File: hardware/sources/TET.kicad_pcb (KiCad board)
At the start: 4 copper layers, 90.2 x 95.9 mm, 80 parts, among them J1 SWT, M1 MountingHole, M2 MountingHole, M3 MountingHole, M4 MountingHole, U1 E80-900M2213S_C42464134, U10 STM32L431RBT6TR, U12 TCAN330GDCNR, U13 SMA_1, U14 SMA_2, U15 8 MHz, U16 5015, U17 5015, U18 5015, U19 INA226AIDGSR, U2 STM32L431CBT6, U20 TLV75533PDBVR, U3 W25Q128JVSIQTR, U4 W25Q128JVSIQTR, U5 W25Q128JVSIQTR, U6 TMP112AIDRLR, U7 TMP112AIDRLR, U8 TMP112AIDRLR, U9 TMP112AIDRLR

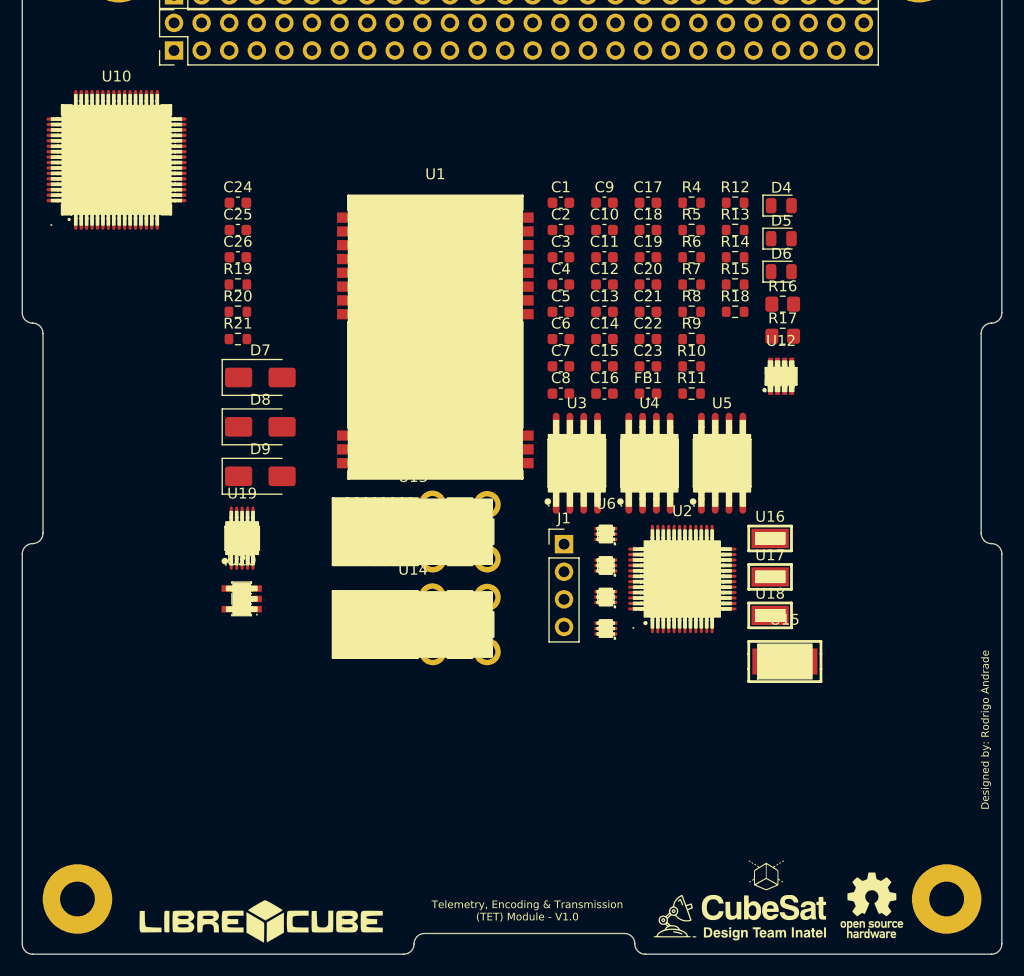
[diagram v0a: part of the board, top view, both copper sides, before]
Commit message: hardware(schematics): upload pre-review schematic
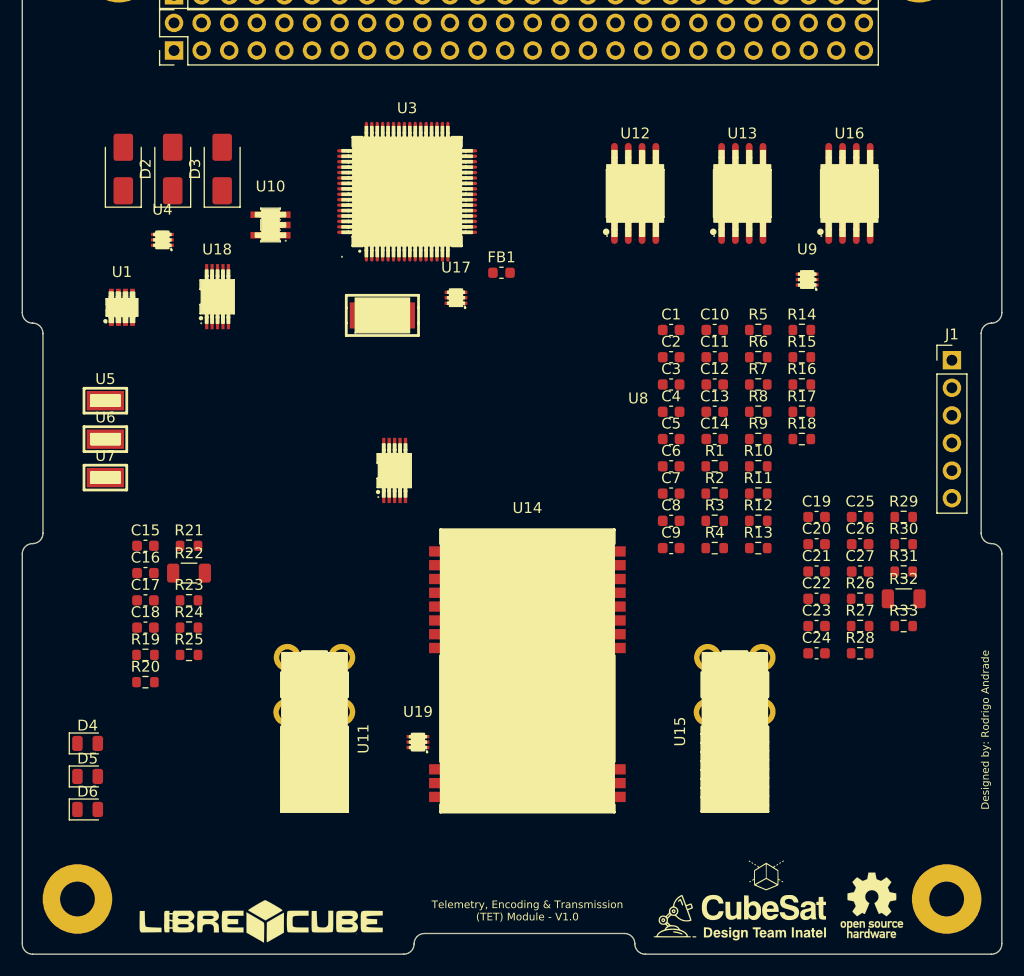
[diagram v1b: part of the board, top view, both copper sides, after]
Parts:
- removed D7, D8, D9: SS14, Diode_SMD:D_SMA
- removed U20: TLV75533PDBVR, TET-Footprints:SOT-23-5_L3.0-W1.7-P0.95-LS2.8-BR
- added C27: 0.1uF, Capacitor_SMD:C_0603_1608Metric, F.Cu at (159.7, 101.9)
- added D1: SS14, Diode_SMD:D_SMA, F.Cu at (91.8, 64.9)
- added D2: SS14, Diode_SMD:D_SMA, F.Cu at (96.4, 64.9)
- added D3: SS14, Diode_SMD:D_SMA, F.Cu at (101.0, 64.9)
- added R1: 10k, Resistor_SMD:R_0603_1608Metric, F.Cu at (146.3, 92.2)
- added R2: 10k, Resistor_SMD:R_0603_1608Metric, F.Cu at (146.3, 94.8)
- added R22: 0.1, Resistor_SMD:R_1206_3216Metric, F.Cu at (97.9, 102.1)
- added R23: 4.7k, Resistor_SMD:R_0603_1608Metric, F.Cu at (97.9, 104.6)
- added R24: 10k, Resistor_SMD:R_0603_1608Metric, F.Cu at (97.9, 107.1)
- added R25: 270, Resistor_SMD:R_0603_1608Metric, F.Cu at (97.9, 109.6)
- added R26: 10k, Resistor_SMD:R_0603_1608Metric, F.Cu at (159.7, 104.4)
- added R27: 10k, Resistor_SMD:R_0603_1608Metric, F.Cu at (159.7, 107.0)
- added R28: 10k, Resistor_SMD:R_0603_1608Metric, F.Cu at (159.7, 109.5)
- added R29: 4.7k, Resistor_SMD:R_0603_1608Metric, F.Cu at (163.7, 96.9)
- added R3: 60, Resistor_SMD:R_0603_1608Metric, F.Cu at (146.3, 97.3)
- added R30: 10k, Resistor_SMD:R_0603_1608Metric, F.Cu at (163.7, 99.4)
- added R31: 10k, Resistor_SMD:R_0603_1608Metric, F.Cu at (163.7, 101.9)
- added R32: 0.1, Resistor_SMD:R_1206_3216Metric, F.Cu at (163.7, 104.4)
- added R33: 4.7k, Resistor_SMD:R_0603_1608Metric, F.Cu at (163.7, 107.0)
- added U11: SMA_1, TET-Footprints:SMA-TH_SMA-KWE_C7498154, F.Cu at (109.4, 112.4)
- C1, C14, C15, C18, C19: value 100nF -> 0.1uF
- C10, C5, C6, C7, C9: value 0.1uF -> 100nF
- C11: value 0.1uF -> 10nF
- C12: value 4.7 nF -> 1uF
- C13: value 22uF -> 1uF
- C16, C17: value 100nF -> 22uF
- C20: value 10uF -> 0.1uF
- C21: value 10nF -> 22uF
- C22, C23: value 1uF -> 100nF
- C25, C26: value 22uF -> 0.1uF
- C3: value 20pF -> 100nF
- C4: value 0.1uF -> 20pF
- C8: value 0.1uF -> 4.7 nF
- D4: value ON_LED -> TX_LED
- D5: value TX_LED -> RX_LED
- D6: value RX_LED -> ON_LED
- J1: value SWT -> SWD; footprint Connector_PinHeader_2.54mm:PinHeader_1x04_P2.54mm_Vertical -> Connector_PinHeader_2.54mm:PinHeader_1x06_P2.54mm_Vertical
- R10: value 200 -> 33
- R11: value 82 -> 33
- R12, R13: value 10k -> 33
- R14: value 10k -> 4.7k
- R15: value 5k -> 10k
- R16: value 60 -> 10k; footprint Resistor_SMD:R_0805_2012Metric_Pad1.20x1.40mm_HandSolder -> Resistor_SMD:R_0603_1608Metric
- R17: value 60 -> 4.7k; footprint Resistor_SMD:R_0805_2012Metric_Pad1.20x1.40mm_HandSolder -> Resistor_SMD:R_0603_1608Metric
- R20: value 0.1 -> 200
- R21: value 10k -> 100
- R4: value 4.7k -> 60
- R5: value 4.7k -> 10k
- R6, R7, R8: value 5k -> 4.7k
- R9: value 270 -> 33
- U1: value E80-900M2213S_C42464134 -> TCAN330GDCNR; footprint TET-Footprints:WIFIM-SMD_22P-L26.0-W16.0-P1.27-TL -> TET-Footprints:SOT-23-8_L2.9-W1.6-P0.65-LS2.8-BL
- U10: value STM32L431RBT6TR -> TLV75533PDBVR; footprint TET-Footprints:LQFP-64_L10.0-W10.0-P0.50-LS12.0-BL -> TET-Footprints:SOT-23-5_L3.0-W1.7-P0.95-LS2.8-BR
- U12: value TCAN330GDCNR -> W25Q128JVSIQTR; footprint TET-Footprints:SOT-23-8_L2.9-W1.6-P0.65-LS2.8-BL -> TET-Footprints:SOIC-8_L5.3-W5.3-P1.27-LS8.0-BL
- U13: value SMA_1 -> W25Q128JVSIQTR; footprint TET-Footprints:SMA-TH_SMA-KWE_C7498154 -> TET-Footprints:SOIC-8_L5.3-W5.3-P1.27-LS8.0-BL
- U14: value SMA_2 -> E80-900M2213S; footprint TET-Footprints:SMA-TH_SMA-KWE_C7498154 -> TET-Footprints:WIFIM-SMD_22P-L26.0-W16.0-P1.27-TL
- U15: value 8 MHz -> SMA_2; footprint TET-Footprints:CRYSTAL-SMD_L5.0-W3.2 -> TET-Footprints:SMA-TH_SMA-KWE_C7498154
- U16: value 5015 -> W25Q128JVSIQTR; footprint TET-Footprints:TEST-SMD_L2.7-W1.0 -> TET-Footprints:SOIC-8_L5.3-W5.3-P1.27-LS8.0-BL
- U17: value 5015 -> TMP112AIDRLR; footprint TET-Footprints:TEST-SMD_L2.7-W1.0 -> TET-Footprints:SOT-563_L1.6-W1.2-P0.50-LS1.6-BR
- U18: value 5015 -> INA226AQDGSRQ1; footprint TET-Footprints:TEST-SMD_L2.7-W1.0 -> TET-Footprints:VSSOP-10_L3.0-W3.0-P0.50-LS4.9-BL
- U19: value INA226AIDGSR -> TMP112AIDRLR; footprint TET-Footprints:MSOP-10_L3.0-W3.0-P0.50-LS5.0-BL -> TET-Footprints:SOT-563_L1.6-W1.2-P0.50-LS1.6-BR
- U2: value STM32L431CBT6 -> 8 MHz; footprint TET-Footprints:LQFP-48_L7.0-W7.0-P0.50-LS9.0-BL -> TET-Footprints:CRYSTAL-SMD_L5.0-W3.2
- U3: value W25Q128JVSIQTR -> STM32L431RBT6TR; footprint TET-Footprints:SOIC-8_L5.3-W5.3-P1.27-LS8.0-BL -> TET-Footprints:LQFP-64_L10.0-W10.0-P0.50-LS12.0-BL
- U4: value W25Q128JVSIQTR -> TMP112AIDRLR; footprint TET-Footprints:SOIC-8_L5.3-W5.3-P1.27-LS8.0-BL -> TET-Footprints:SOT-563_L1.6-W1.2-P0.50-LS1.6-BR
- U5: value W25Q128JVSIQTR -> 5015; footprint TET-Footprints:SOIC-8_L5.3-W5.3-P1.27-LS8.0-BL -> TET-Footprints:TEST-SMD_L2.7-W1.0
- U6, U7: value TMP112AIDRLR -> 5015; footprint TET-Footprints:SOT-563_L1.6-W1.2-P0.50-LS1.6-BR -> TET-Footprints:TEST-SMD_L2.7-W1.0
- U8: value TMP112AIDRLR -> INA226AQDGSRQ1; footprint TET-Footprints:SOT-563_L1.6-W1.2-P0.50-LS1.6-BR -> TET-Footprints:VSSOP-10_L3.0-W3.0-P0.50-LS4.9-BL
- moved D4 80.8 mm to (88.6, 117.8)
- moved D5 80.8 mm to (88.6, 120.8)
- moved D6 80.8 mm to (88.6, 123.8)
- moved C24 67.5 mm to (155.7, 109.5)
- moved C25 63.1 mm to (159.7, 96.9)
- moved C26 63.1 mm to (159.7, 99.4)
- moved C17 59.0 mm to (93.9, 104.6)
- moved C18 59.0 mm to (93.9, 107.1)
- moved U18 58.7 mm to (100.5, 76.6)
- moved U5 57.1 mm to (90.2, 86.2)
- moved U4 49.3 mm to (95.4, 71.4)
- moved U6 46.9 mm to (90.2, 89.8)
- moved U7 46.8 mm to (90.2, 93.3)
- moved C15 45.4 mm to (93.9, 99.6)
- moved C16 45.4 mm to (93.9, 102.1)
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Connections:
- C1 pad 1: /NRST -> +3.3V
- C11 pad 1: +3.3V -> +3.3VA
- C12 pad 1: Net-(C12-Pad1) -> +3.3VA
- C15 pad 1: /LR_RST -> +3.3V
- C16 pad 1: +3.3V -> Net-(U10-IN)
- C2 pad 1: /OSC_IN -> Net-(U2-OSC2)
- C21 pad 1: +3.3VA -> Net-(U14-VCC)
- C22 pad 1: +3.3VA -> Net-(U14-VCC)
- C23 pad 1: +3.3V -> /LR_RST
- C25 pad 1: Net-(U20-IN) -> +3.3V
- C3 pad 1: /OSC_OUT -> +3.3V
- C4 pad 1: +3.3V -> Net-(U2-OSC1)
- C6 pad 1: +3.3V -> /NRST
- C8 pad 1: +3.3V -> Net-(C8-Pad1)
- D4 pad 2: +3.3V -> /TX_LED
- D5 pad 2: /TX_LED -> /RX_LED
- D6 pad 2: /RX_LED -> +3.3V
- J1 pad 4: GND -> /NRST
- R10 pad 1: GND -> Net-(U3-PA6)
- R10 pad 2: Net-(D5-K) -> /QSPI_IO3
- R11 pad 1: GND -> Net-(U3-PA7)
- R11 pad 2: Net-(D6-K) -> /QSPI_IO2
- R12 pad 1: +3.3V -> Net-(U3-PB0)
- R12 pad 2: /FLASH1_CS -> /QSPI_IO1
- R13 pad 1: +3.3V -> Net-(U3-PB1)
- R13 pad 2: /FLASH2_CS -> /QSPI_IO0
- R14 pad 2: /FLASH3_CS -> /I2C1_SDA
- R15 pad 2: /TMP112_D_ALERT -> /FLASH1_CS
- R16 pad 1: /CAN_A_H -> +3.3V
- R16 pad 2: Net-(C12-Pad1) -> /FLASH2_CS
- R17 pad 1: Net-(C12-Pad1) -> +3.3V
- R17 pad 2: /CAN_A_L -> /I2C2_SDA
- R18 pad 2: /LR_RST -> /FLASH3_CS
- R19 pad 2: /Power_Supply/INA226_ALERT -> /PWR_INA_ALERT
- R20 pad 1: /Power_Supply/SENSE+ -> GND
- R20 pad 2: /Power_Supply/SENSE- -> Net-(D4-K)
- R21 pad 1: Net-(U20-IN) -> GND
- R21 pad 2: Net-(U20-EN) -> Net-(D5-K)
- R4 pad 1: +3.3V -> Net-(C8-Pad1)
- R4 pad 2: /SCL0 -> /CAN_A_L
- R5 pad 1: +3.3V -> GND
- R5 pad 2: /SDA0 -> Net-(U3-PH3/BOOT0)
- R6 pad 2: /TMP112_C_ALERT -> /TMP_B_ALERT
- R7 pad 2: /TMP112_B_ALERT -> /I2C1_SCL
- R8 pad 2: /TMP112_A_ALERT -> /I2C2_SCL
- R9 pad 1: GND -> Net-(U3-PA3)
- R9 pad 2: Net-(D4-K) -> /QSPI_CLK
- U1 pad 1: GND -> /CAN1_TX
- U1 pad 2: unconnected-(U1-NC-Pad2) -> GND
- U1 pad 3: /MISO -> +3.3V
- U1 pad 4: /MOSI -> /CAN1_RX
- U1 pad 5: /SCK -> GND
- U1 pad 6: /NSS -> /CAN_A_L
- U1 pad 7: /LR_BUSY -> /CAN_A_H
- U1 pad 8: GND -> /CAN1_STB
- U10 pad 1: unconnected-(U10-VBAT-Pad1) -> Net-(U10-IN)
- U10 pad 2: unconnected-(U10-PC13-Pad2) -> GND
- U10 pad 3: unconnected-(U10-PC14/OSC32_IN-Pad3) -> Net-(U10-EN)
- U10 pad 5: unconnected-(U10-PH0/OSCIN-Pad5) -> +3.3V
- U12 pad 1: /CAN1_TX -> /FLASH1_CS
- U12 pad 2: GND -> /QSPI_IO1
- U12 pad 3: +3.3V -> /QSPI_IO2
- U12 pad 4: /CAN1_RX -> GND
- U12 pad 5: GND -> /QSPI_IO0
- U12 pad 6: /CAN_A_L -> /QSPI_CLK
- U12 pad 7: /CAN_A_H -> /QSPI_IO3
- U12 pad 8: /CAN1_STB -> +3.3V
- U13 pad 1: GND -> /FLASH3_CS
- U13 pad 2: GND -> /QSPI_IO1
- U13 pad 3: GND -> /QSPI_IO2
- U13 pad 5: /ANT_2.4 -> /QSPI_IO0
- U14 pad 2: GND -> unconnected-(U14-NC-Pad2)
- U14 pad 3: GND -> /SPI1_MISO
- U14 pad 4: GND -> /SPI1_MOSI
- U14 pad 5: /ANT_LORA -> /SPI1_SCK
- U15 pad 1: /OSC_OUT -> GND
- U15 pad 2: /OSC_IN -> GND
- U16 pad 1: +3.3V -> /FLASH2_CS
- U17 pad 1: +5V -> /I2C2_SDA
- U19 pad 1: GND -> /I2C2_SCL
- U19 pad 3: /Power_Supply/INA226_ALERT -> /TMP_C_ALERT
- U19 pad 4: /Power_Supply/SDA0 -> /I2C2_SDA
- U19 pad 5: /Power_Supply/SCL0 -> +3.3V
- U19 pad 6: +3.3V -> /I2C2_SDA
- U2 pad 1: +3.3V -> Net-(U2-OSC1)
- U2 pad 2: unconnected-(U2-PC13-Pad2) -> Net-(U2-OSC2)
- U3 pad 1: /FLASH1_CS -> +3.3V
- U3 pad 2: /QSPI_IO1 -> /LR_IO9
- U3 pad 3: /QSPI_IO2 -> unconnected-(U3-PC14/OSC32_IN-Pad3)
- U3 pad 4: GND -> unconnected-(U3-PC15/OSC32_OUT-Pad4)
- U3 pad 5: /QSPI_IO0 -> Net-(U2-OSC2)
- U3 pad 6: /QSPI_CLK -> Net-(U2-OSC1)
- U3 pad 7: /QSPI_IO3 -> /NRST
- U3 pad 8: +3.3V -> /TX_LED
- U4 pad 1: /FLASH2_CS -> /I2C1_SCL
- U4 pad 2: /QSPI_IO1 -> GND
- U4 pad 3: /QSPI_IO2 -> /TMP_B_ALERT
- U4 pad 4: GND -> +3.3V
- U4 pad 5: /QSPI_IO0 -> +3.3V
- U4 pad 6: /QSPI_CLK -> /I2C1_SDA
- U5 pad 1: /FLASH3_CS -> +3.3V
- U6 pad 1: /I2C1_SCL -> +5V
- U7 pad 1: /I2C1_SCL -> GND
- U8 pad 1: /I2C1_SCL -> GND
- U8 pad 3: /TMP112_D_ALERT -> /PWR_INA_ALERT
- U8 pad 5: +3.3V -> /I2C1_SCL
- U8 pad 6: /I2C1_SDA -> +3.3V
- U9 pad 3: /TMP112_A_ALERT -> /TMP_A_ALERT

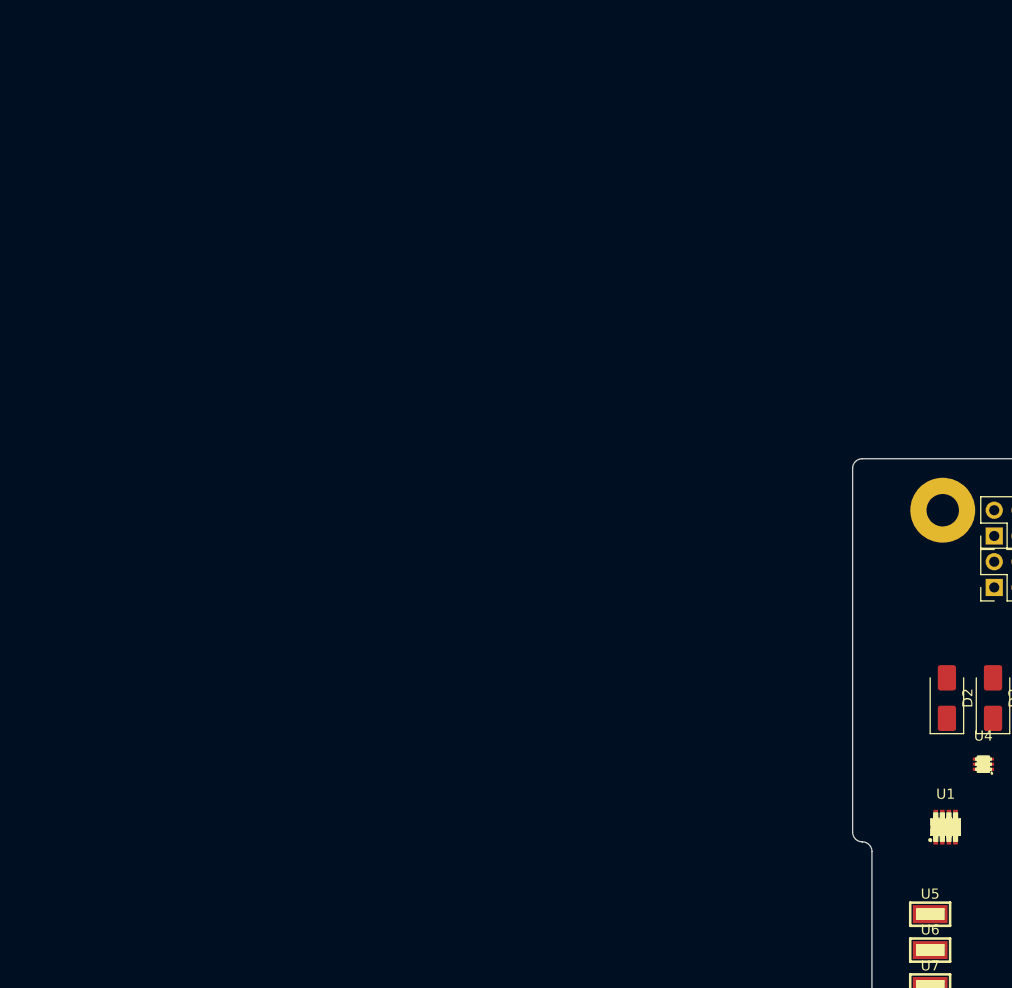
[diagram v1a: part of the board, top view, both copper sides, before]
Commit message: hardware(schematic): link datasheet to all main components #1
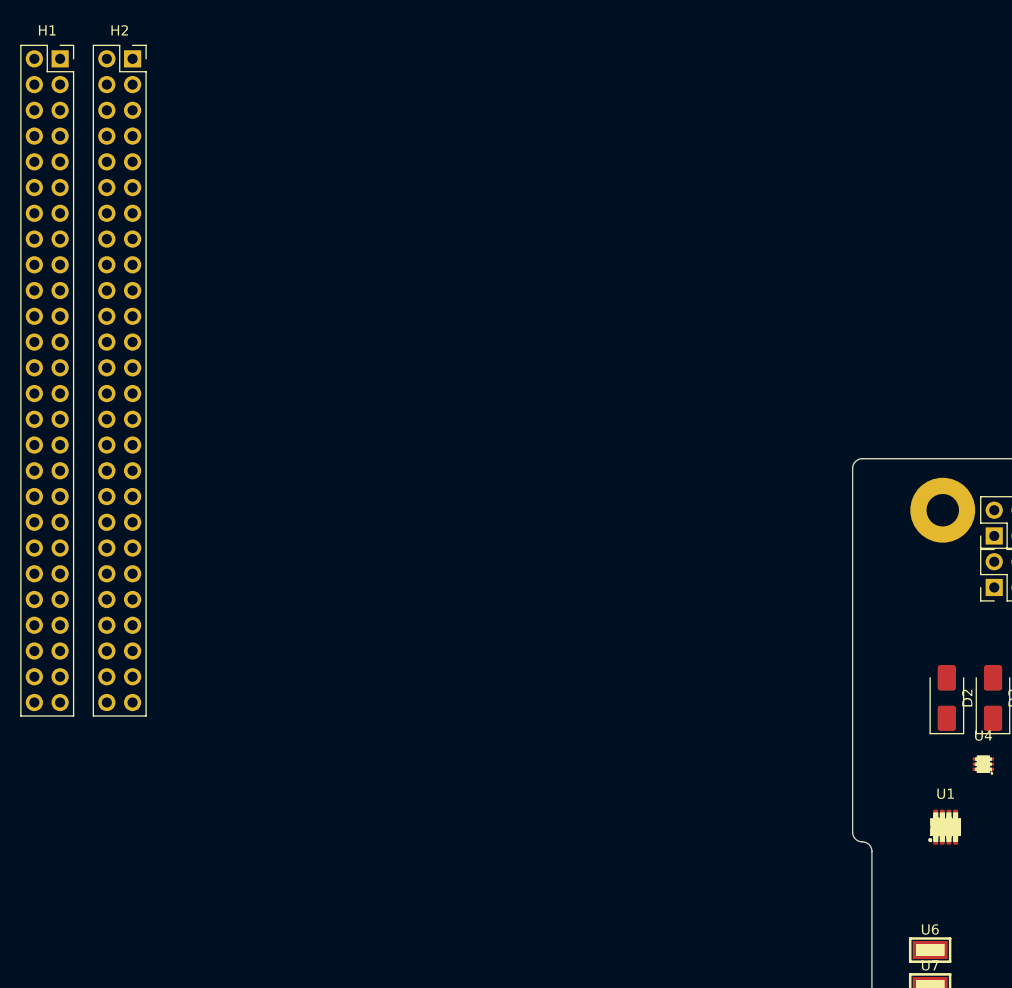
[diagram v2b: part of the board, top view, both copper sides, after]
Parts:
- removed U5: 5015, TET-Footprints:TEST-SMD_L2.7-W1.0
- added H1: PC/104 Connector, Connector_PinSocket_2.54mm:PinSocket_2x26_P2.54mm_Vertical, F.Cu at (4.37, 1.82)
- added H2: PC/104 Connector, Connector_PinSocket_2.54mm:PinSocket_2x26_P2.54mm_Vertical, F.Cu at (11.5, 1.82)
